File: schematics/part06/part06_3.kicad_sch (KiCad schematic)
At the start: 27 parts, among them SW1 RESET, SW2 STEP, SW3 RUN, U1 8088, U10 LCD 4x20, U11 82C84, U12 8259A-2, U13 8254, U2 74HC573, U3 74HC573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

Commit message: Added files for part 8
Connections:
- net D0: now also U10.7 (DB0)
- net D1: now also U10.8 (DB1)
- net D2: now also U10.9 (DB2)
- net D3: now also U10.10 (DB3)
- net D4: now also U10.11 (DB4)
- net D5: now also U10.12 (DB5)
- net D6: now also U10.13 (DB6)
- net D7: now also U10.14 (DB7)
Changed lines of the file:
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@@
     (stroke (width 0) (type default) (color 0 0 0 0))
   )
-  (wire (pts (xy 297.18 245.11) (xy 325.12 245.11))
-    (stroke (width 0) (type default) (color 0 0 0 0))
-  )
   (wire (pts (xy 73.66 267.97) (xy 138.43 267.97))
     (stroke (width 0) (type default) (color 0 0 0 0))
@@
     (stroke (width 0) (type default) (color 0 0 0 0))
   )
-  (wire (pts (xy 297.18 260.35) (xy 325.12 260.35))
+  (wire (pts (xy 294.64 260.35) (xy 325.12 260.35))
     (stroke (width 0) (type default) (color 0 0 0 0))
   )
@@
     (stroke (width 0) (type default) (color 0 0 0 0))
   )
-  (wire (pts (xy 297.18 262.89) (xy 325.12 262.89))
+  (wire (pts (xy 294.64 262.89) (xy 325.12 262.89))
     (stroke (width 0) (type default) (color 0 0 0 0))
   )
@@
     (stroke (width 0) (type default) (color 0 0 0 0))
   )
-  (wire (pts (xy 297.18 257.81) (xy 325.12 257.81))
+  (wire (pts (xy 294.64 257.81) (xy 325.12 257.81))
     (stroke (width 0) (type default) (color 0 0 0 0))
   )
@@
     (stroke (width 0) (type default) (color 0 0 0 0))
   )
+  (wire (pts (xy 294.64 245.11) (xy 325.12 245.11))
+    (stroke (width 0) (type default) (color 0 0 0 0))
+  )
   (wire (pts (xy 256.54 217.17) (xy 260.35 217.17))
     (stroke (width 0) (type default) (color 0 0 0 0))
@@
     (stroke (width 0) (type default) (color 0 0 0 0))
   )
+  (wire (pts (xy 294.64 247.65) (xy 325.12 247.65))
+    (stroke (width 0) (type default) (color 0 0 0 0))
+  )
   (bus (pts (xy 254 219.71) (xy 254 222.25))
     (stroke (width 0) (type default) (color 0 0 0 0))
@@
     (stroke (width 0) (type default) (color 0 0 0 0))
   )
-  (wire (pts (xy 297.18 252.73) (xy 325.12 252.73))
+  (wire (pts (xy 294.64 252.73) (xy 325.12 252.73))
     (stroke (width 0) (type default) (color 0 0 0 0))
   )
@@
     (stroke (width 0) (type default) (color 0 0 0 0))
   )
+  (wire (pts (xy 294.64 250.19) (xy 325.12 250.19))
+    (stroke (width 0) (type default) (color 0 0 0 0))
+  )
   (wire (pts (xy 233.68 189.23) (xy 231.14 189.23))
     (stroke (width 0) (type default) (color 0 0 0 0))
@@
     (stroke (width 0) (type default) (color 0 0 0 0))
   )
-  (wire (pts (xy 297.18 247.65) (xy 325.12 247.65))
-    (stroke (width 0) (type default) (color 0 0 0 0))
-  )
   (wire (pts (xy 205.74 224.79) (xy 213.36 224.79))
     (stroke (width 0) (type default) (color 0 0 0 0))
@@
     (stroke (width 0) (type default) (color 0 0 0 0))
   )
-  (wire (pts (xy 297.18 250.19) (xy 325.12 250.19))
-    (stroke (width 0) (type default) (color 0 0 0 0))
-  )
   (wire (pts (xy 167.64 231.14) (xy 167.64 233.68))
     (stroke (width 0) (type default) (color 0 0 0 0))
@@
     (stroke (width 0) (type default) (color 0 0 0 0))
   )
-  (wire (pts (xy 297.18 255.27) (xy 325.12 255.27))
+  (wire (pts (xy 294.64 255.27) (xy 325.12 255.27))
     (stroke (width 0) (type default) (color 0 0 0 0))
   )
@@
       (effects (font (size 1.27 1.27)) hide)
     )
+    (pin "1")
+    (pin "2")
+    (pin "3")
     (pin "4")
     (pin "5")
     (pin "6")
+    (pin "10")
+    (pin "8")
+    (pin "9")
+    (pin "11")
+    (pin "12")
+    (pin "13")
+    (pin "14")
+    (pin "7")
   )
   (symbol (lib_id "power:GND") (at 224.79 156.21 0) (unit 1)
@@
     (pin "2")
     (pin "3")
+    (pin "4")
+    (pin "5")
+    (pin "6")
+    (pin "10")
+    (pin "8")
+    (pin "9")
+    (pin "11")
+    (pin "12")
+    (pin "13")
+    (pin "14")
+    (pin "7")
   )
   (symbol (lib_id "power:GND") (at 58.42 205.74 0) (unit 1)
@@
     (pin "2")
     (pin "3")
+    (pin "4")
+    (pin "5")
+    (pin "6")
+    (pin "10")
+    (pin "8")
+    (pin "9")
+    (pin "11")
+    (pin "12")
+    (pin "13")
+    (pin "14")
+    (pin "7")
   )
   (symbol (lib_id "power:GND") (at 184.15 124.46 0) (unit 1)
@@
       (effects (font (size 1.27 1.27)) hide)
     )
+    (pin "1")
+    (pin "2")
+    (pin "3")
     (pin "4")
     (pin "5")
     (pin "6")
+    (pin "10")
+    (pin "8")
+    (pin "9")
+    (pin "11")
+    (pin "12")
+    (pin "13")
+    (pin "14")
+    (pin "7")
   )
   (symbol (lib_id "power:+5V") (at 209.55 115.57 0) (unit 1)
@@
       (effects (font (size 1.27 1.27)) hide)
     )
+    (pin "1")
+    (pin "2")
+    (pin "3")
+    (pin "4")
+    (pin "5")
+    (pin "6")
     (pin "10")
     (pin "8")
     (pin "9")
+    (pin "11")
+    (pin "12")
+    (pin "13")
+    (pin "14")
+    (pin "7")
   )
   (symbol (lib_id "Device:R") (at 24.13 256.54 0) (mirror y) (unit 1)
@@
       (effects (font (size 1.27 1.27)) hide)
     )
+    (pin "1")
+    (pin "2")
+    (pin "3")
+    (pin "4")
+    (pin "5")
+    (pin "6")
+    (pin "10")
+    (pin "8")
+    (pin "9")
     (pin "11")
     (pin "12")
     (pin "13")
+    (pin "14")
+    (pin "7")
   )
   (symbol (lib_id "74xx:74HC02") (at 313.69 237.49 0) (mirror x) (unit 4)
@@
       (effects (font (size 1.27 1.27)) hide)
     )
+    (pin "1")
+    (pin "2")
+    (pin "3")
+    (pin "4")
+    (pin "5")
+    (pin "6")
+    (pin "10")
+    (pin "8")
+    (pin "9")
     (pin "11")
     (pin "12")
     (pin "13")
+    (pin "14")
+    (pin "7")
   )
   (symbol (lib_id "power:+5V") (at 58.42 223.52 0) (unit 1)

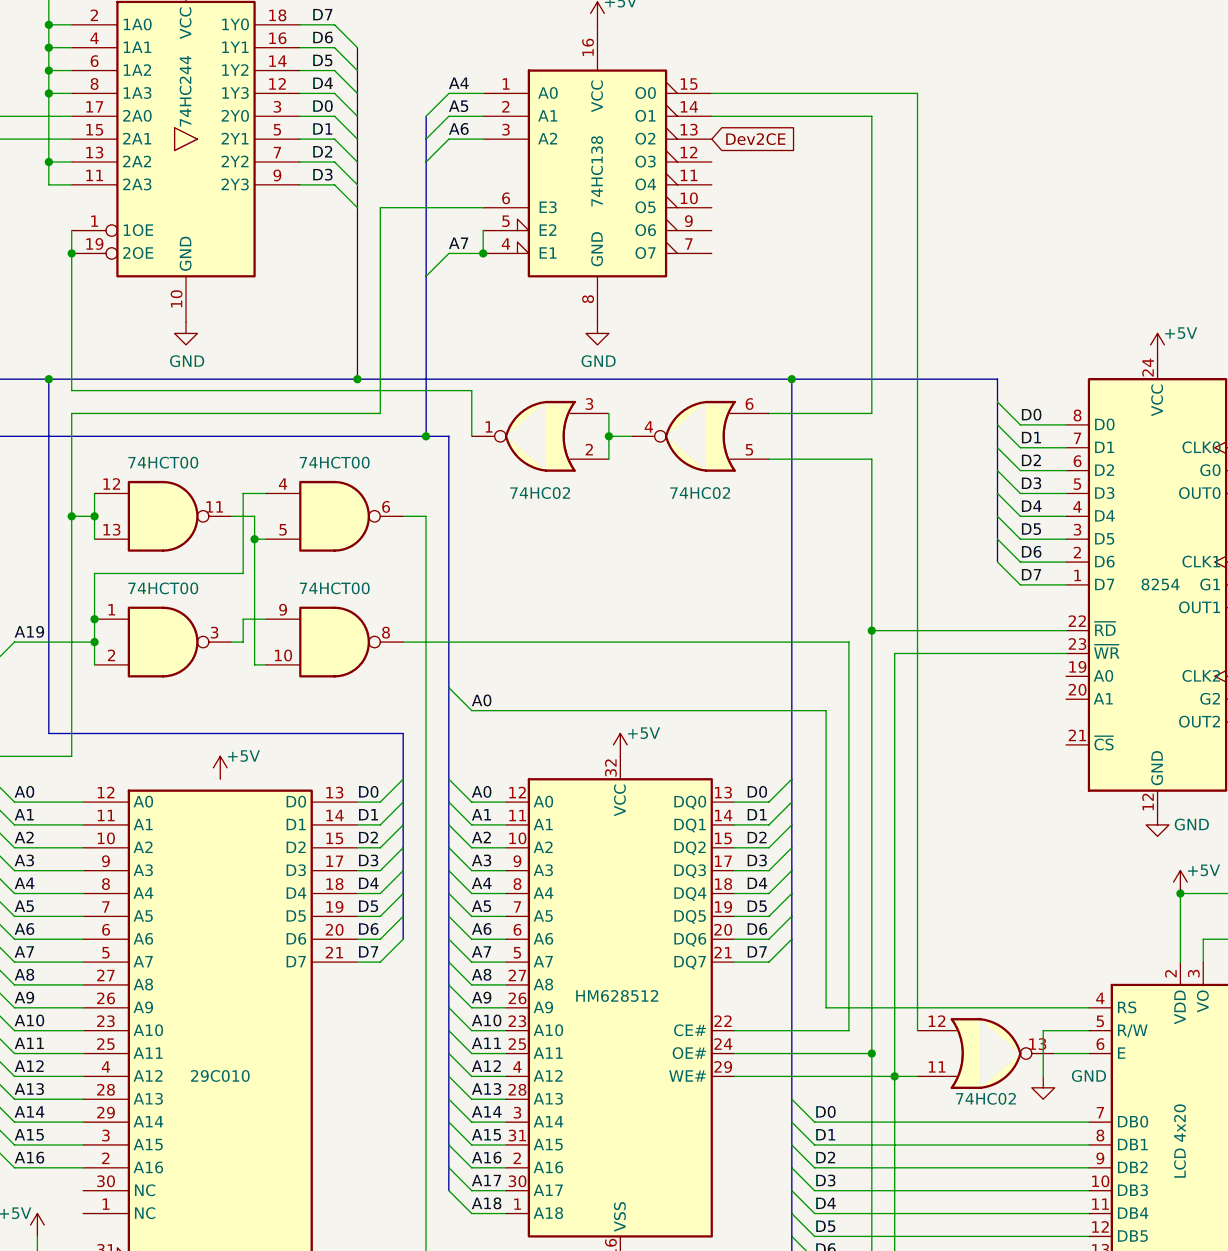
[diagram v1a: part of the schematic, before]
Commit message: Fixed errors in schematics. Thanks Greg for spotting these.
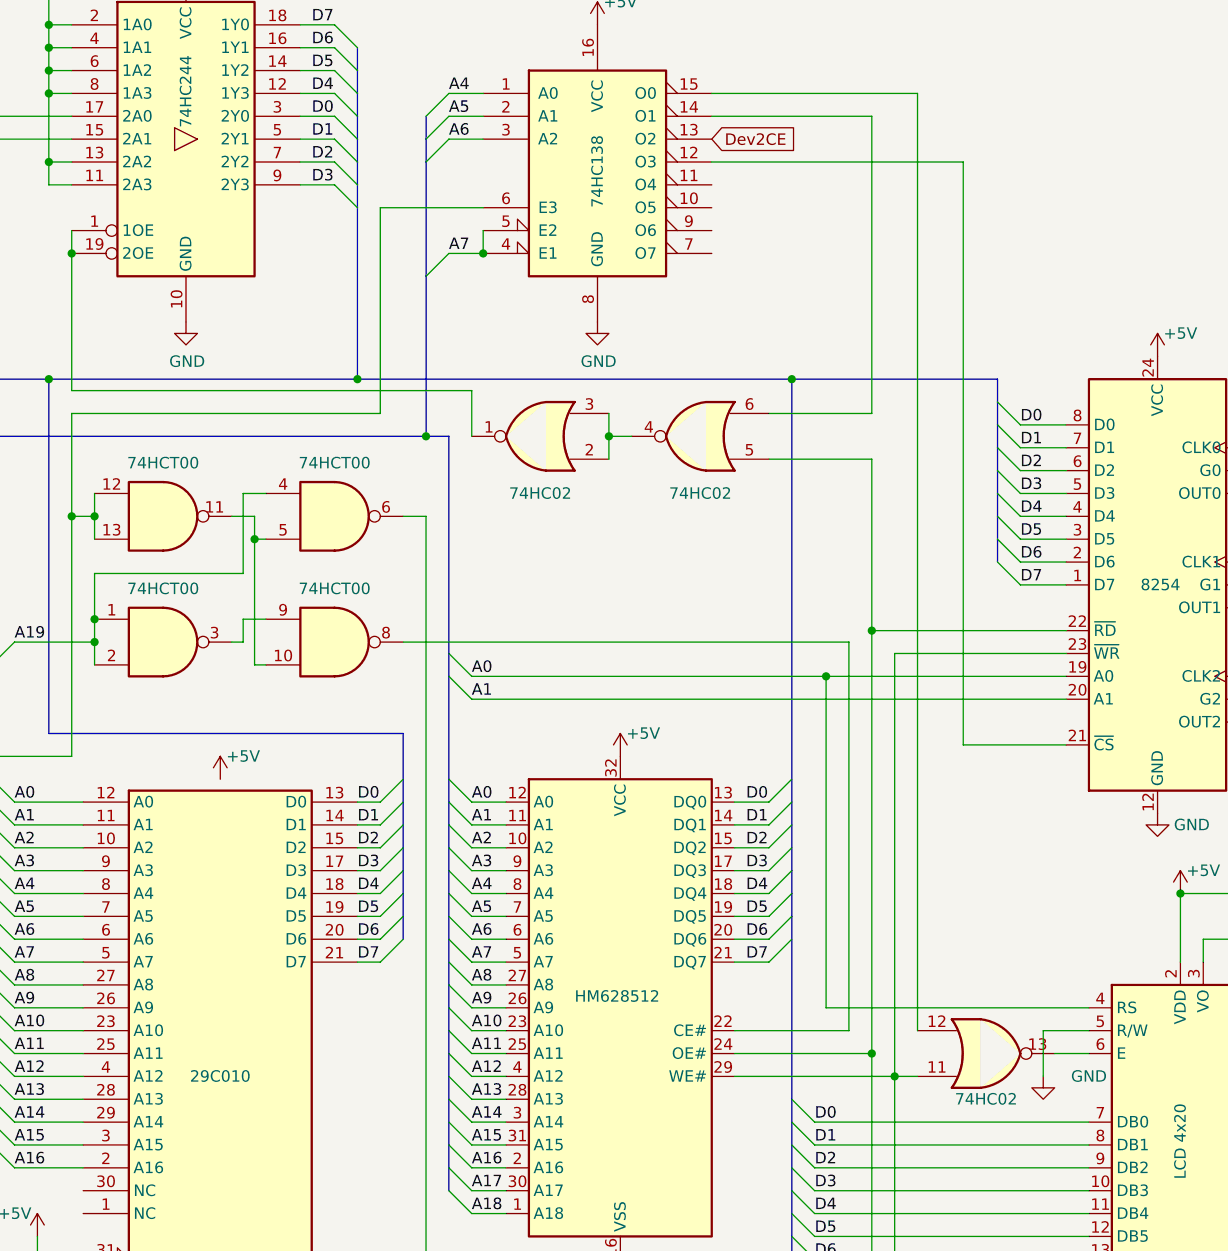
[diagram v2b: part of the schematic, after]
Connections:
- net A0: now also U13.19 (A0)
- net A1: now also U13.20 (A1)
- net at U8.12 (O3): now also U13.21 (~{CS})
